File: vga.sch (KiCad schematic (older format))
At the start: 7 parts, among them J17 DB15HD_Female

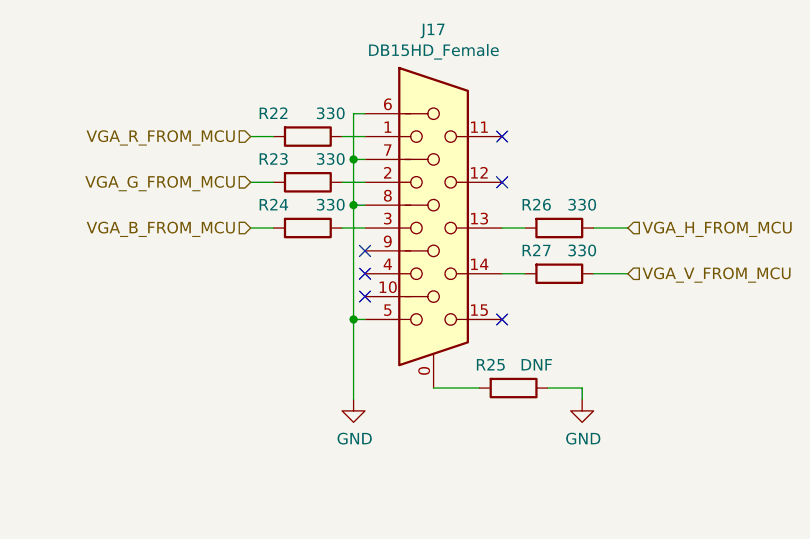
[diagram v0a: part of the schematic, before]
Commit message: Cleaned up Atmega reset. Set hold size to 3.5mm, so M3 screws go through nicely Reset numbering to page x 100 Renamed Launchpad to EK-TM4C123GXL Renamed top-level signals to KBMS page as KBMS_TO/FROM_MCU
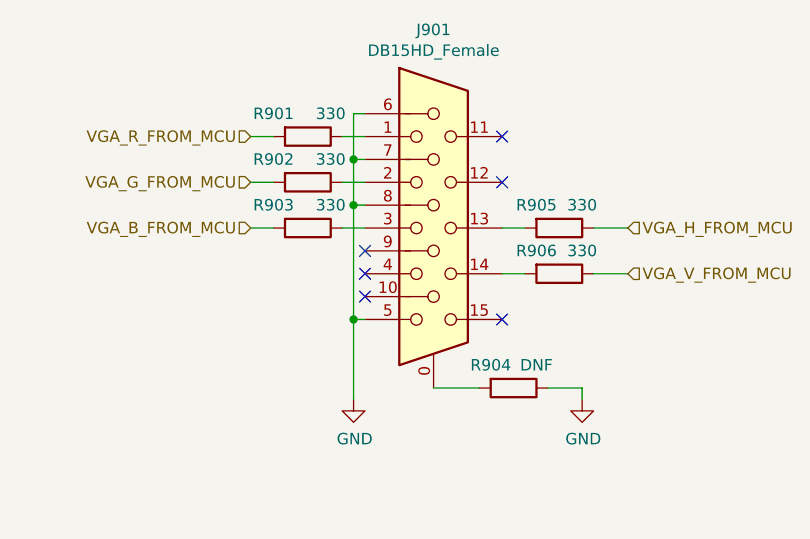
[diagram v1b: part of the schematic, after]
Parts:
- renumbered J17 to J901, R22 to R901, R23 to R902, R24 to R903, R25 to R904, R26 to R905, R27 to R906
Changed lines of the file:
@@
 P 5550 3250
 AR Path="/5DF388AB" Ref="J?"  Part="1"
-AR Path="/5DF25A09/5DF388AB" Ref="J17"  Part="1"
-F 0 "J17" H 5550 4117 50  0000 C CNN
+AR Path="/5DF25A09/5DF388AB" Ref="J901"  Part="1"
+F 0 "J901" H 5550 4117 50  0000 C CNN
 F 1 "DB15HD_Female" H 5550 4026 50  0000 C CNN
 F 2 "Connector_Dsub:DSUB-15-HD_Female_Horizontal_P2.29x1.98mm_EdgePinOffset3.03mm_Housed_MountingHolesOffset4.94mm" H 4600 3650 50  0001 C CNN
@@
 VGA_V_FROM_MCU
 $Comp
-L Device:R R27
+L Device:R R906
 U 1 1 5E020EF6
 P 6100 3450
-F 0 "R27" V 6000 3350 50  0000 C CNN
+F 0 "R906" V 6000 3350 50  0000 C CNN
 F 1 "330" V 6000 3550 50  0000 C CNN
 F 2 "Resistor_THT:R_Axial_DIN0207_L6.3mm_D2.5mm_P10.16mm_Horizontal" V 6030 3450 50  0001 C CNN
@@
 $EndComp
 $Comp
-L Device:R R26
+L Device:R R905
 U 1 1 5E02143C
 P 6100 3250
-F 0 "R26" V 6000 3150 50  0000 C CNN
+F 0 "R905" V 6000 3150 50  0000 C CNN
 F 1 "330" V 6000 3350 50  0000 C CNN
 F 2 "Resistor_THT:R_Axial_DIN0207_L6.3mm_D2.5mm_P10.16mm_Horizontal" V 6030 3250 50  0001 C CNN
@@
 $EndComp
 $Comp
-L Device:R R22
+L Device:R R901
 U 1 1 5E021698
 P 5000 2850
-F 0 "R22" V 4900 2700 50  0000 C CNN
+F 0 "R901" V 4900 2700 50  0000 C CNN
 F 1 "330" V 4900 2950 50  0000 C CNN
 F 2 "Resistor_THT:R_Axial_DIN0207_L6.3mm_D2.5mm_P10.16mm_Horizontal" V 4930 2850 50  0001 C CNN
@@
 $EndComp
 $Comp
-L Device:R R23
+L Device:R R902
 U 1 1 5E021BC3
 P 5000 3050
-F 0 "R23" V 4900 2900 50  0000 C CNN
+F 0 "R902" V 4900 2900 50  0000 C CNN
 F 1 "330" V 4900 3150 50  0000 C CNN
 F 2 "Resistor_THT:R_Axial_DIN0207_L6.3mm_D2.5mm_P10.16mm_Horizontal" V 4930 3050 50  0001 C CNN
@@
 $EndComp
 $Comp
-L Device:R R24
+L Device:R R903
 U 1 1 5E021E5E
 P 5000 3250
-F 0 "R24" V 4900 3100 50  0000 C CNN
+F 0 "R903" V 4900 3100 50  0000 C CNN
 F 1 "330" V 4900 3350 50  0000 C CNN
 F 2 "Resistor_THT:R_Axial_DIN0207_L6.3mm_D2.5mm_P10.16mm_Horizontal" V 4930 3250 50  0001 C CNN
@@
 $EndComp
 $Comp
-L Device:R R25
+L Device:R R904
 U 1 1 5E3BC4C1
 P 5900 3950
-F 0 "R25" V 5800 3850 50  0000 C CNN
+F 0 "R904" V 5800 3850 50  0000 C CNN
 F 1 "DNF" V 5800 4050 50  0000 C CNN
 F 2 "Resistor_THT:R_Axial_DIN0207_L6.3mm_D2.5mm_P10.16mm_Horizontal" V 5830 3950 50  0001 C CNN
